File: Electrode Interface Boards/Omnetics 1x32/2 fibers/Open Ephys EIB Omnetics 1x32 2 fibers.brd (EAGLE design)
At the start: 16.5 x 16.5 mm, 41 parts

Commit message: Fix unconnected trace on 1x32 EIB
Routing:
- net S$39: track 3.74 -> 4.42 mm
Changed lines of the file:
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@@
 </signal>
 <signal name="S$39">
-<wire x1="28.575" y1="18.923" x2="28.575" y2="19.3675" width="0.2032" layer="1"/>
+<wire x1="27.813" y1="18.542" x2="28.575" y2="19.3675" width="0.2032" layer="1"/>
 <wire x1="28.575" y1="19.3675" x2="28.7655" y2="19.558" width="0.2032" layer="1"/>
 <wire x1="28.7655" y1="19.558" x2="28.7655" y2="20.447" width="0.2032" layer="1"/>

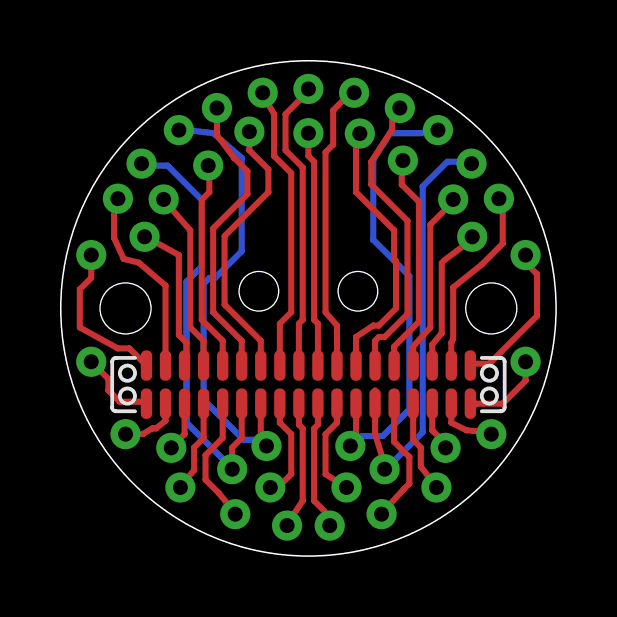
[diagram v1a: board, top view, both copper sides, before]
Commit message: Update design for bilateral drive
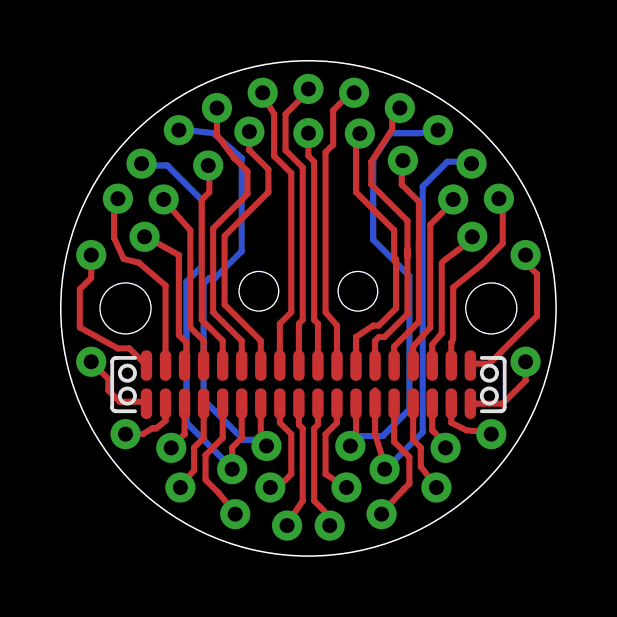
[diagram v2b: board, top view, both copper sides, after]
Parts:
- renumbered U$28 to S$41
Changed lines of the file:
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@@
 <grid distance="2.5" unitdist="mil" unit="mil" style="lines" multiple="1" display="yes" altdistance="0.005" altunitdist="inch" altunit="inch"/>
 <layers>
-<layer number="1" name="Top" color="11" fill="1" visible="yes" active="yes"/>
-<layer number="16" name="Bottom" color="1" fill="1" visible="yes" active="yes"/>
-<layer number="17" name="Pads" color="2" fill="1" visible="yes" active="yes"/>
-<layer number="18" name="Vias" color="2" fill="1" visible="yes" active="yes"/>
-<layer number="19" name="Unrouted" color="6" fill="1" visible="yes" active="yes"/>
-<layer number="20" name="Dimension" color="15" fill="1" visible="yes" active="yes"/>
+<layer number="1" name="Top" color="11" fill="1" visible="no" active="yes"/>
+<layer number="16" name="Bottom" color="1" fill="1" visible="no" active="yes"/>
+<layer number="17" name="Pads" color="2" fill="1" visible="no" active="yes"/>
+<layer number="18" name="Vias" color="2" fill="1" visible="no" active="yes"/>
+<layer number="19" name="Unrouted" color="6" fill="1" visible="no" active="yes"/>
+<layer number="20" name="Dimension" color="15" fill="1" visible="no" active="yes"/>
 <layer number="21" name="tPlace" color="8" fill="1" visible="no" active="yes"/>
 <layer number="22" name="bPlace" color="14" fill="1" visible="no" active="yes"/>
-<layer number="23" name="tOrigins" color="15" fill="1" visible="yes" active="yes"/>
+<layer number="23" name="tOrigins" color="15" fill="1" visible="no" active="yes"/>
 <layer number="24" name="bOrigins" color="15" fill="1" visible="no" active="yes"/>
 <layer number="25" name="tNames" color="7" fill="1" visible="no" active="yes"/>
@@
 <layer number="28" name="bValues" color="7" fill="1" visible="no" active="yes"/>
 <layer number="29" name="tStop" color="7" fill="3" visible="yes" active="yes"/>
-<layer number="30" name="bStop" color="7" fill="6" visible="no" active="yes"/>
+<layer number="30" name="bStop" color="7" fill="6" visible="yes" active="yes"/>
 <layer number="31" name="tCream" color="7" fill="4" visible="no" active="yes"/>
 <layer number="32" name="bCream" color="7" fill="5" visible="no" active="yes"/>
@@
 <layer number="42" name="bRestrict" color="1" fill="10" visible="no" active="yes"/>
 <layer number="43" name="vRestrict" color="2" fill="10" visible="no" active="yes"/>
-<layer number="44" name="Drills" color="7" fill="1" visible="yes" active="yes"/>
-<layer number="45" name="Holes" color="7" fill="1" visible="yes" active="yes"/>
+<layer number="44" name="Drills" color="7" fill="1" visible="no" active="yes"/>
+<layer number="45" name="Holes" color="7" fill="1" visible="no" active="yes"/>
 <layer number="46" name="Milling" color="3" fill="1" visible="no" active="yes"/>
 <layer number="47" name="Measures" color="7" fill="1" visible="no" active="yes"/>
 <layer number="48" name="Document" color="7" fill="1" visible="no" active="yes"/>
 <layer number="49" name="Reference" color="7" fill="1" visible="no" active="yes"/>
-<layer number="51" name="tDocu" color="3" fill="1" visible="yes" active="yes"/>
+<layer number="51" name="tDocu" color="3" fill="1" visible="no" active="yes"/>
 <layer number="52" name="bDocu" color="7" fill="1" visible="no" active="yes"/>
 <layer number="91" name="Nets" color="2" fill="1" visible="no" active="no"/>
@@
 <circle x="19.304" y="25.4" radius="1.27" width="0.1778" layer="51"/>
 <circle x="31.496" y="25.4" radius="1.27" width="0.1778" layer="51"/>
-<rectangle x1="24.4475" y1="21.971" x2="25.654" y2="22.479" layer="30"/>
 <circle x="23.7236" y="25.9715" radius="1.016" width="0.1778" layer="51"/>
 <text x="23.90175" y="27.350096875" size="0.762" layer="51" font="vector" ratio="12">open-
@@
 </class>
 </classes>
-<designrules name="default *">
+<designrules name="Fusion_eagle_rule_v1.1">
 <description language="de">&lt;b&gt;EAGLE Design Rules&lt;/b&gt;
 &lt;p&gt;
@@
 necessary adjustments and save your customized
 design rules under a new name.</description>
+<description language="zh">&lt;b&gt;Seeed Studio EAGLE Design Rules&lt;/b&gt;
+</description>
 <param name="layerSetup" value="(1*16)"/>
 <param name="mtCopper" value="0.035mm 0.035mm 0.035mm 0.035mm 0.035mm 0.035mm 0.035mm 0.035mm 0.035mm 0.035mm 0.035mm 0.035mm 0.035mm 0.035mm 0.035mm 0.035mm"/>
@@
 <param name="mdPadVia" value="6mil"/>
 <param name="mdViaVia" value="6mil"/>
-<param name="mdSmdPad" value="6mil"/>
-<param name="mdSmdVia" value="6mil"/>
-<param name="mdSmdSmd" value="6mil"/>
+<param name="mdSmdPad" value="0mil"/>
+<param name="mdSmdVia" value="0mil"/>
+<param name="mdSmdSmd" value="0mil"/>
 <param name="mdViaViaSameLayer" value="8mil"/>
 <param name="mnLayersViaInSmd" value="2"/>
-<param name="mdCopperDimension" value="8mil"/>
-<param name="mdDrill" value="6mil"/>
+<param name="mdCopperDimension" value="10mil"/>
+<param name="mdDrill" value="10mil"/>
 <param name="mdSmdStop" value="0mil"/>
 <param name="msWidth" value="6mil"/>
-<param name="msDrill" value="20mil"/>
-<param name="msMicroVia" value="9.99mm"/>
+<param name="msDrill" value="12mil"/>
+<param name="msMicroVia" value="12mil"/>
 <param name="msBlindViaRatio" value="0.5"/>
 <param name="rvPadTop" value="0.25"/>
@@
 <param name="rlMinPadBottom" value="10mil"/>
 <param name="rlMaxPadBottom" value="20mil"/>
-<param name="rlMinViaOuter" value="8mil"/>
+<param name="rlMinViaOuter" value="6mil"/>
 <param name="rlMaxViaOuter" value="20mil"/>
-<param name="rlMinViaInner" value="8mil"/>
+<param name="rlMinViaInner" value="6mil"/>
 <param name="rlMaxViaInner" value="20mil"/>
 <param name="rlMinMicroViaOuter" value="4mil"/>
@@
 <param name="psTop" value="-1"/>
 <param name="psBottom" value="-1"/>
-<param name="psFirst" value="-1"/>
+<param name="psFirst" value="0"/>
 <param name="psElongationLong" value="100"/>
 <param name="psElongationOffset" value="100"/>
 <param name="mvStopFrame" value="1"/>
 <param name="mvCreamFrame" value="0"/>
-<param name="mlMinStopFrame" value="4mil"/>
-<param name="mlMaxStopFrame" value="4mil"/>
+<param name="mlMinStopFrame" value="2mil"/>
+<param name="mlMaxStopFrame" value="2mil"/>
 <param name="mlMinCreamFrame" value="0mil"/>
 <param name="mlMaxCreamFrame" value="0mil"/>
-<param name="mlViaStopLimit" value="0mil"/>
+<param name="mlViaStopLimit" value="100mil"/>
 <param name="srRoundness" value="0"/>
 <param name="srMinRoundness" value="0mil"/>
@@
 <param name="checkAngle" value="0"/>
 <param name="checkFont" value="1"/>
-<param name="checkRestrict" value="1"/>
+<param name="checkRestrict" value="0"/>
 <param name="useDiameter" value="13"/>
 <param name="maxErrors" value="50"/>
@@
 <element name="U$26" library="josh" package="LARGEGOLDPIN" value="GOLDPINLARGE" x="21.1328" y="19.431"/>
 <element name="U$27" library="josh" package="LARGEGOLDPIN" value="GOLDPINLARGE" x="23.4315" y="31.2928"/>
-<element name="U$28" library="josh" package="LARGEGOLDPIN" value="GOLDPINLARGE" x="29.972" y="20.7518"/>
+<element name="S$41" library="josh" package="LARGEGOLDPIN" value="GOLDPINLARGE" x="29.972" y="20.7518"/>
 <element name="U$29" library="josh" package="LARGEGOLDPIN" value="GOLDPINLARGE" x="22.352" y="32.0802"/>
 <element name="U$32" library="josh" package="LARGEGOLDPIN" value="GOLDPINLARGE" x="22.9616" y="18.542"/>
@@
 <wire x1="27.559" y1="24.8285" x2="27.7495" y2="24.8285" width="0.2032" layer="1"/>
 <wire x1="27.7495" y1="24.8285" x2="28.321" y2="25.4" width="0.2032" layer="1"/>
-<wire x1="28.321" y1="25.4" x2="28.321" y2="26.9875" width="0.2032" layer="1"/>
+<wire x1="28.321" y1="25.4" x2="28.321" y2="27.051" width="0.2032" layer="1"/>
 </signal>
 <signal name="S$9">
@@
 <wire x1="27.7495" y1="24.4475" x2="27.94" y2="24.4475" width="0.2032" layer="1"/>
 <wire x1="27.94" y1="24.4475" x2="28.702" y2="25.2095" width="0.2032" layer="1"/>
-<wire x1="28.702" y1="25.2095" x2="28.702" y2="27.051" width="0.2032" layer="1"/>
+<wire x1="28.702" y1="25.2095" x2="28.702" y2="27.3685" width="0.2032" layer="1"/>
 </signal>
 <signal name="S$10">
@@
 <wire x1="28.2575" y1="23.749" x2="28.2575" y2="24.13" width="0.2032" layer="1"/>
 <wire x1="28.2575" y1="24.13" x2="29.083" y2="24.9555" width="0.2032" layer="1"/>
-<wire x1="29.083" y1="24.9555" x2="29.083" y2="27.178" width="0.2032" layer="1"/>
+<wire x1="29.083" y1="24.9555" x2="29.083" y2="27.6225" width="0.2032" layer="1"/>
 </signal>
 <signal name="S$11">
